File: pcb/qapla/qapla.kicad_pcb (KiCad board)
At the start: 2 copper layers, 153.1 x 125.4 mm, 63 parts

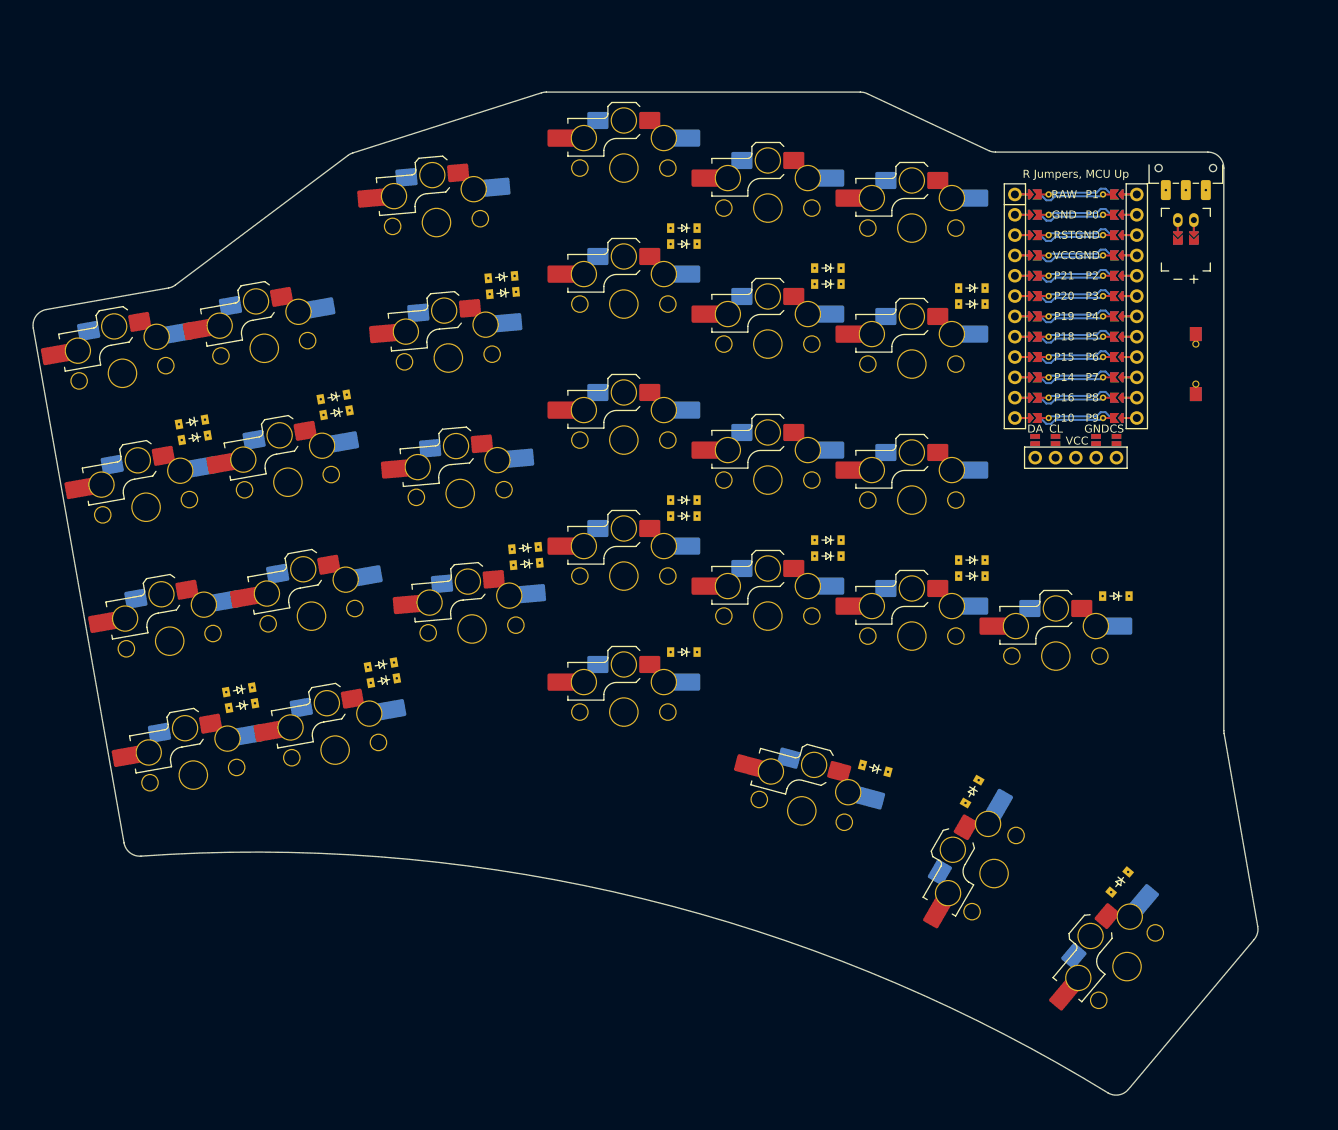
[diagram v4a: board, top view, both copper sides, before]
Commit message: All components in place except mounting holes
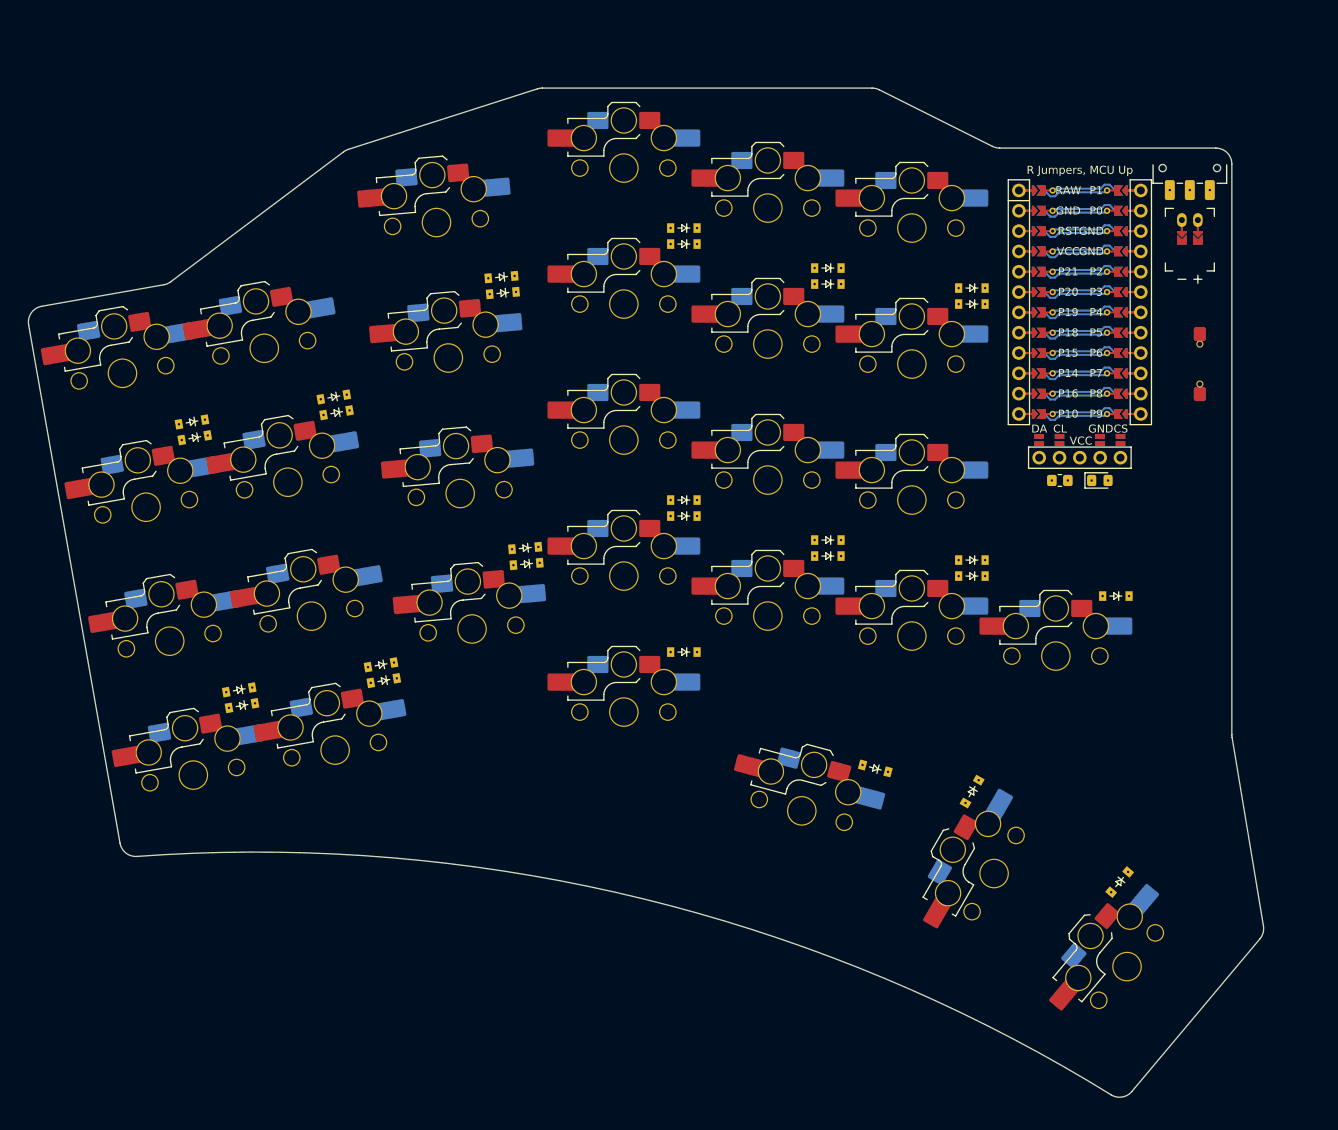
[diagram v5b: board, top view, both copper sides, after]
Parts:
- added _3: , D_0805_2012Metric_Pad1.15x1.40mm_HandSolder, F.Cu at (232.4, 76.8)
- added _3: , R_0805_2012Metric_Pad1.20x1.40mm_HandSolder, F.Cu at (232.4, 76.8)
- moved MCU1 0.71 mm to (232.4, 53.2)
- moved DISP1 0.50 mm to (232.4, 57.2)
- moved JST1 0.50 mm to (246.1, 44.2)
- moved _1 0.50 mm to (247.4, 62.2)
- moved _2 0.50 mm to (246.1, 37.7)
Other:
- board size 153.1 x 125.4 mm -> 154.4 x 126.1 mm

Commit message: Adding mounting holes
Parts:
- added MH1: , ceoloide:mounting_hole_npth, F.Cu at (138.7, 46.6)
- added MH2: , ceoloide:mounting_hole_npth, F.Cu at (157.5, 107.3)
- added MH3: , ceoloide:mounting_hole_npth, F.Cu at (211.4, 33.2)
- added MH4: , ceoloide:mounting_hole_npth, F.Cu at (211.4, 108.2)
- added MH5: , ceoloide:mounting_hole_npth, F.Cu at (245.1, 98.7)
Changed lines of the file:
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@@
 (net 87 "JST1_2")
 (net 88 "_3_1")
+  (footprint "ceoloide:mounting_hole_npth"
+    (layer "F.Cu")
+    (at 138.7031687 46.6227519 10)
+    (property "Reference" "MH1"
+      (at 0 2.55 10)
+      (layer "F.SilkS")
+      hide
+      (effects (font (size 1 1) (thickness 0.15)))
+    )
+    (pad "" np_thru_hole circle
+      (at 0 0 10)
+      (size 3.2 3.2)
+      (drill 3.2)
+      (layers "*.Cu" "*.Mask")
+    )
+  )
+  (footprint "ceoloide:mounting_hole_npth"
+    (layer "F.Cu")
+    (at 157.46152419999999 107.3063443 5)
+    (property "Reference" "MH2"
+      (at 0 2.55 5)
+      (layer "F.SilkS")
+      hide
+      (effects (font (size 1 1) (thickness 0.15)))
+    )
+    (pad "" np_thru_hole circle
+      (at 0 0 5)
+      (size 3.2 3.2)
+      (drill 3.2)
+      (layers "*.Cu" "*.Mask")
+    )
+  )
+  (footprint "ceoloide:mounting_hole_npth"
+    (layer "F.Cu")
+    (at 211.3930287 33.237541 0)
+    (property "Reference" "MH3"
+      (at 0 2.55 0)
+      (layer "F.SilkS")
+      hide
+      (effects (font (size 1 1) (thickness 0.15)))
+    )
+    (pad "" np_thru_hole circle
+      (at 0 0 0)
+      (size 3.2 3.2)
+      (drill 3.2)
+      (layers "*.Cu" "*.Mask")
+    )
+  )
+  (footprint "ceoloide:mounting_hole_npth"
+    (layer "F.Cu")
+    (at 211.3930287 108.237541 0)
+    (property "Reference" "MH4"
+      (at 0 2.55 0)
+      (layer "F.SilkS")
+      hide
+      (effects (font (size 1 1) (thickness 0.15)))
+    )
+    (pad "" np_thru_hole circle
+      (at 0 0 0)
+      (size 3.2 3.2)
+      (drill 3.2)
+      (layers "*.Cu" "*.Mask")
+    )
+  )
+  (footprint "ceoloide:mounting_hole_npth"
+    (layer "F.Cu")
+    (at 245.1430287 98.7375409 0)
+    (property "Reference" "MH5"
+      (at 0 2.55 0)
+      (layer "F.SilkS")
+      hide
+      (effects (font (size 1 1) (thickness 0.15)))
+    )
+    (pad "" np_thru_hole circle
+      (at 0 0 0)
+      (size 3.2 3.2)
+      (drill 3.2)
+      (layers "*.Cu" "*.Mask")
+    )
+  )
   (footprint "ceoloide:switch_choc_v1_v2"
     (layer "B.Cu")

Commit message: Adding holes for display plate
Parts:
- added MH6: , ceoloide:mounting_hole_npth, F.Cu at (225.4, 84.7)
- added MH7: , ceoloide:mounting_hole_npth, F.Cu at (247.9, 84.7)
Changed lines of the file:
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@@
     (pad "4" thru_hole roundrect (at -1.5 0) (size 1.2 1.4) (drill 0.3) (layers "*.Cu" "*.Paste" "*.Mask") (roundrect_rratio 0.208333) (net 88 "_3_1"))
+  )
+  (footprint "ceoloide:mounting_hole_npth"
+    (layer "F.Cu")
+    (at 225.3930287 84.7375409 0)
+    (property "Reference" "MH6"
+      (at 0 2.55 0)
+      (layer "F.SilkS")
+      hide
+      (effects (font (size 1 1) (thickness 0.15)))
+    )
+    (pad "" np_thru_hole circle
+      (at 0 0 0)
+      (size 2.2 2.2)
+      (drill 2.2)
+      (layers "*.Cu" "*.Mask")
+    )
+  )
+  (footprint "ceoloide:mounting_hole_npth"
+    (layer "F.Cu")
+    (at 247.8930287 84.7375409 0)
+    (property "Reference" "MH7"
+      (at 0 2.55 0)
+      (layer "F.SilkS")
+      hide
+      (effects (font (size 1 1) (thickness 0.15)))
+    )
+    (pad "" np_thru_hole circle
+      (at 0 0 0)
+      (size 2.2 2.2)
+      (drill 2.2)
+      (layers "*.Cu" "*.Mask")
+    )
   )
   (gr_line (start 112.41612146766047 122.13354750570238) (end 100.99025906060282 57.33426183375843) (layer Edge.Cuts) (stroke (width 0.15) (type default)))

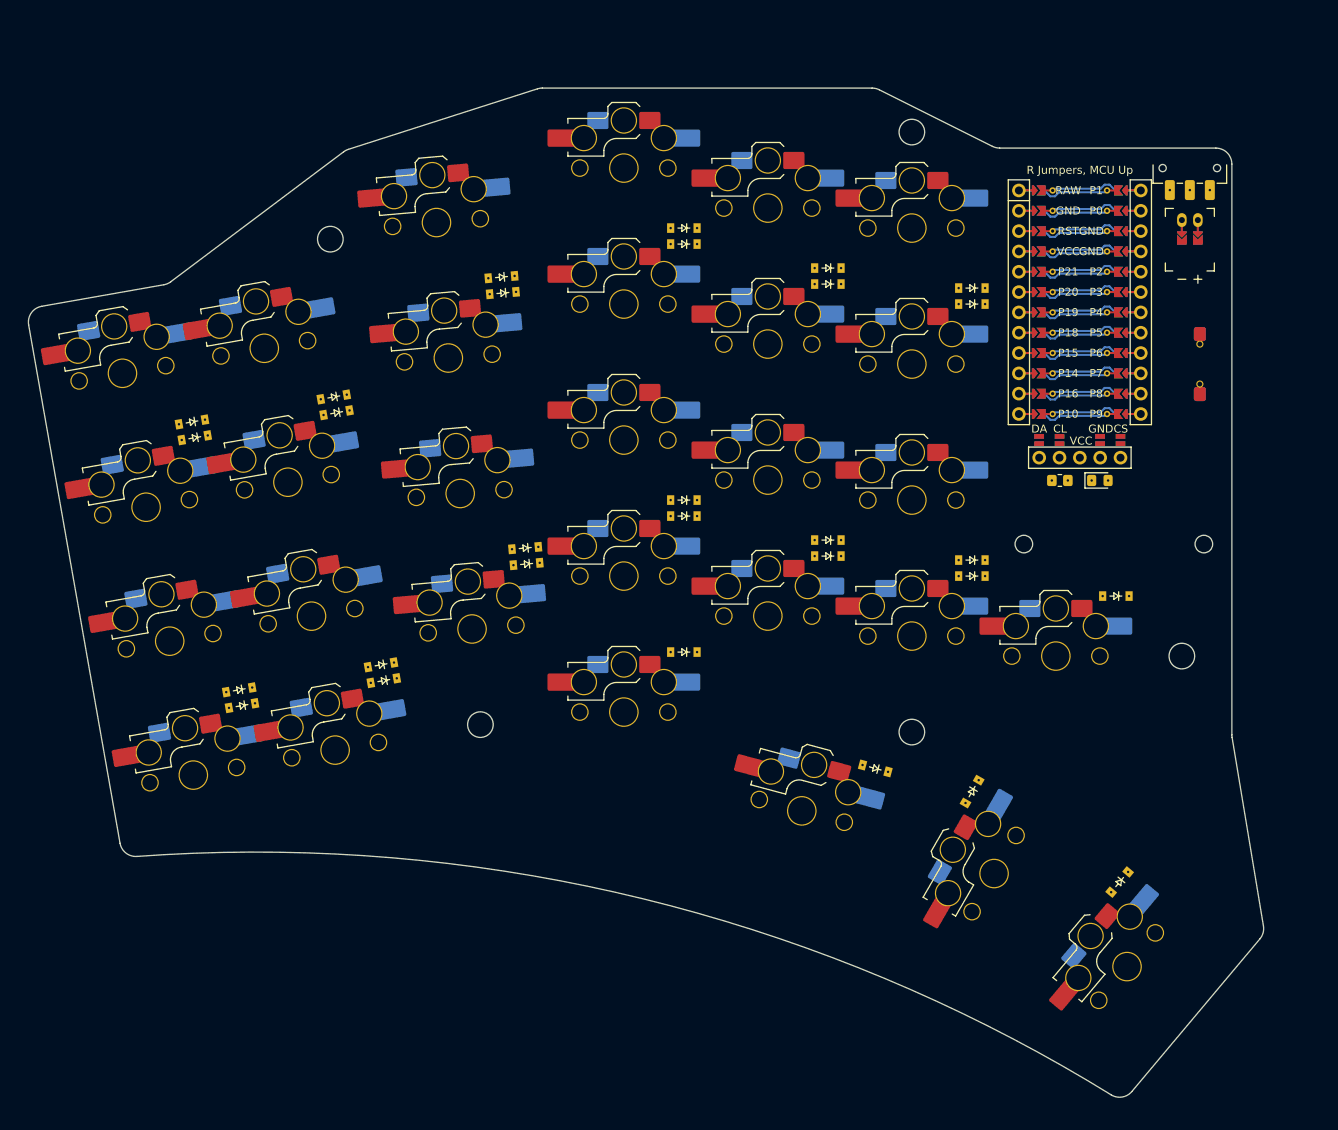
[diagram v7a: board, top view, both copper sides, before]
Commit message: Adding bottom plate
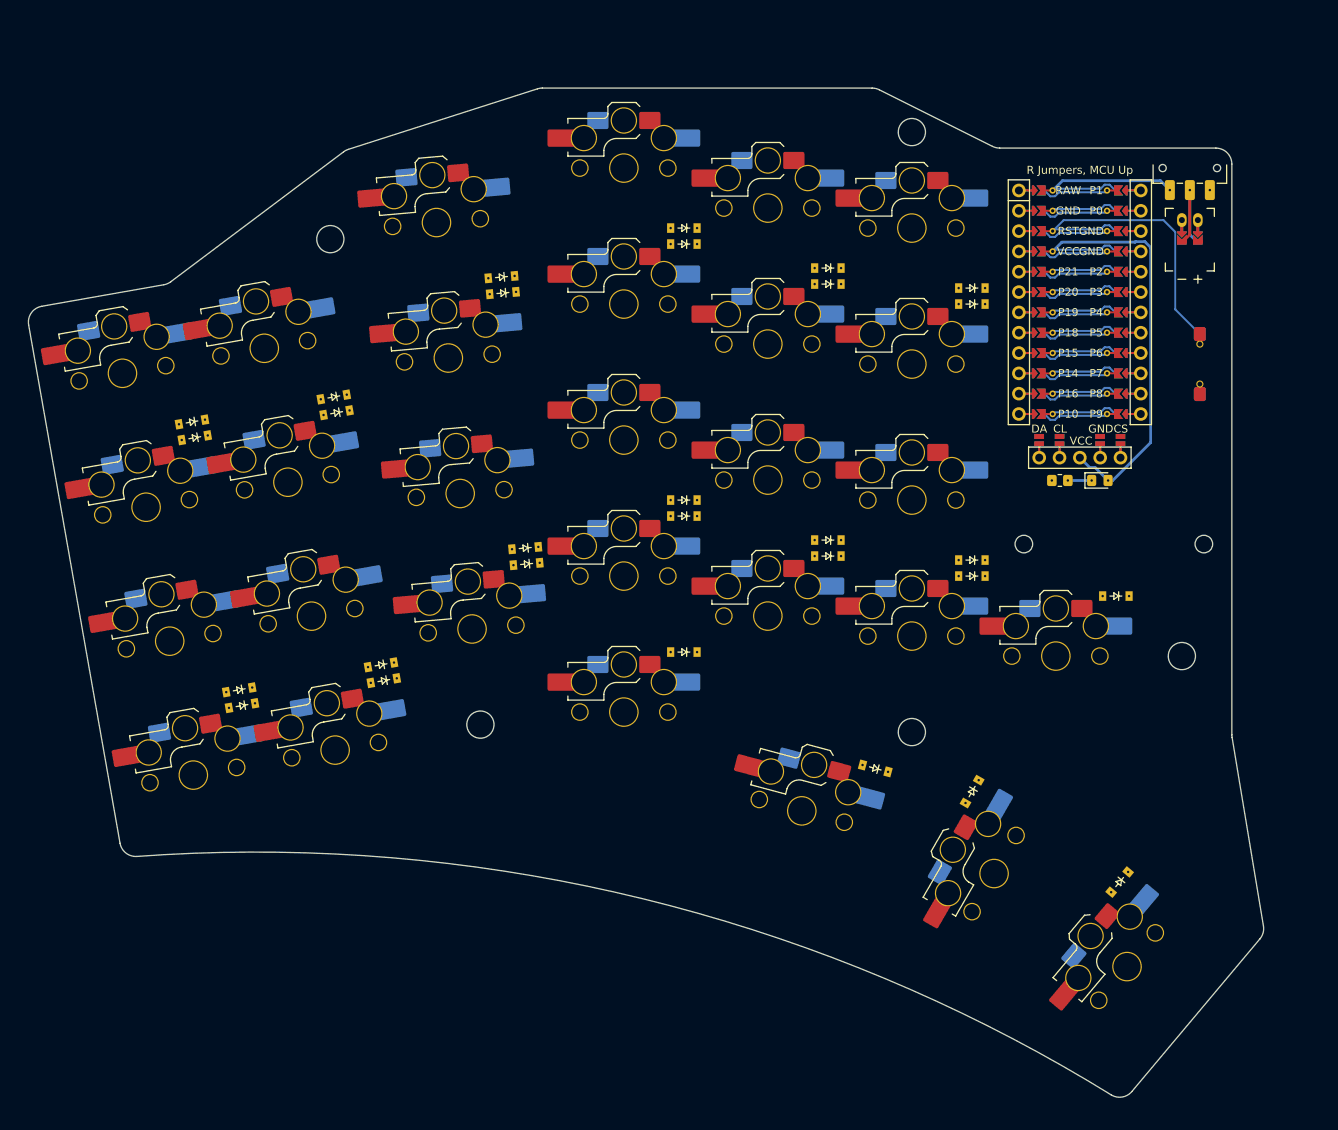
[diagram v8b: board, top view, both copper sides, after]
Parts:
- removed the _3 at (232.4, 76.8) (x2)
- added _3: , R_0805_2012Metric_Pad1.20x1.40mm_HandSolder, F.Cu at (232.4, 76.8)
- added _3: , D_0805_2012Metric_Pad1.15x1.40mm_HandSolder, F.Cu at (232.4, 76.8)
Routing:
- net (no net): track 337.7 -> 0.00 mm
- net VCC: track 0.00 -> 59.3 mm
- net RST: track 0.00 -> 40.4 mm
- net GND: track 0.00 -> 29.5 mm
- net RAW: track 0.00 -> 25.5 mm
- net BAT_P: track 0.00 -> 14.0 mm
- net P10: track 0.00 -> 9.84 mm
- net P21: track 0.00 -> 9.84 mm
- net P20: track 0.00 -> 9.84 mm
- net P19: track 0.00 -> 9.84 mm
- net P18: track 0.00 -> 9.84 mm
- net P16: track 0.00 -> 9.84 mm
- net P15: track 0.00 -> 9.84 mm
- net P14: track 0.00 -> 9.84 mm
- net P8: track 0.00 -> 9.83 mm
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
